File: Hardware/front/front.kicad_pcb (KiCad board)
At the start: 4 copper layers, 177 x 62 mm, 67 parts, among them J102 Conn_02x25_Counter_Clockwise, J301 Conn_02x25_Counter_Clockwise, Q301 2N7002E, Q302 2N7002E, SW201 B3W-9002-Y1C, SW202 B3W-9002-Y1C, SW203 B3W-9002-Y1C, SW204 B3W-9002-Y1C, SW205 B3W-9000-RHG2C, SW206 B3W-9002-G1G, SW207 TT EN11, U101 XRA1203, U102 AT24CS32-XHM, U103 PCA9955B, U201 74LV14, U202 74LVC1G14GV

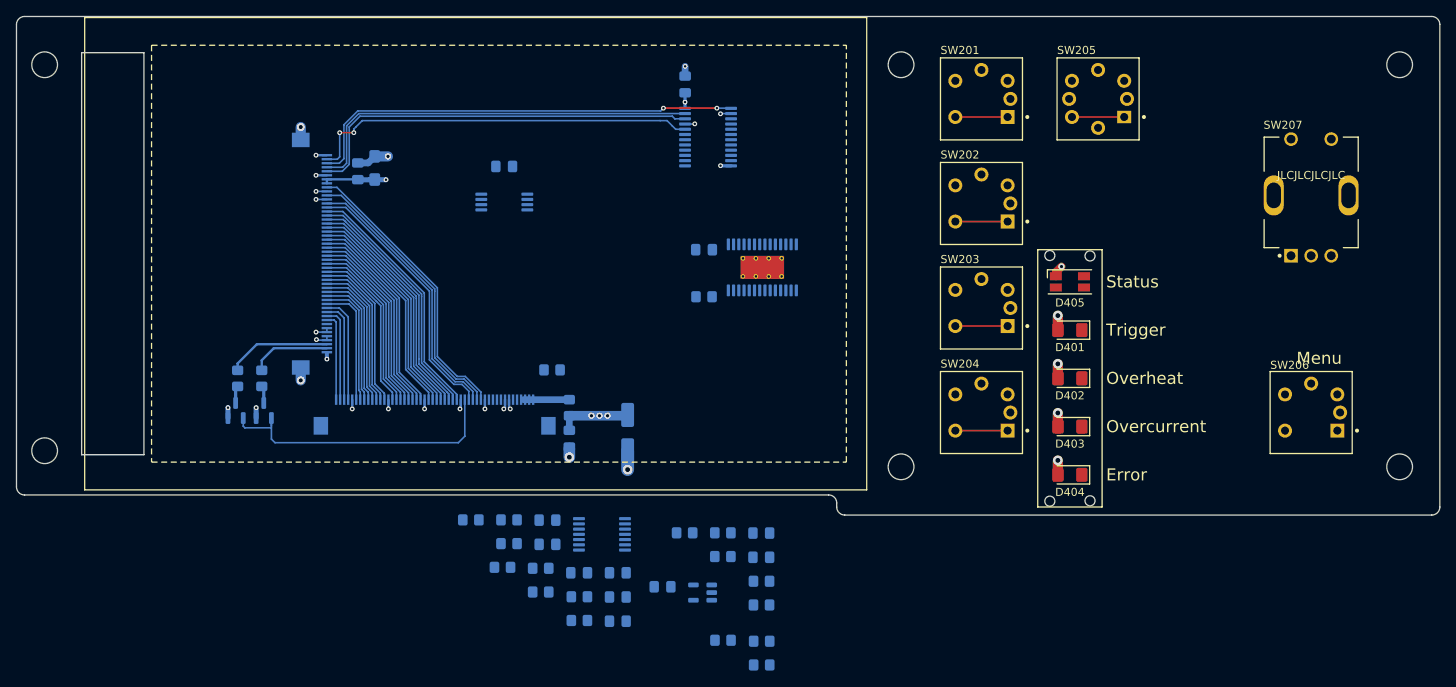
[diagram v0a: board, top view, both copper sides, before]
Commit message: More reworking of the controller and friends
- Add more rear IO to the controller, in this case finishing positioning
  of the Ethernet jack, and adding a suitable right angle USB B jack
  (USB C is preferrable but there's basically no jacks that are
  sufficiently long)

- Mostly finish power section on controller (save for the enable input
  for our +3V3 rail; it'll be slaved off the SoM +3V3 rail)

- Minor tweaks to pinout of FFC connector on front panel

- Update cutout shape of analog board

- Fixed a few footprints metadata

- Add footprints for further rear panel IO
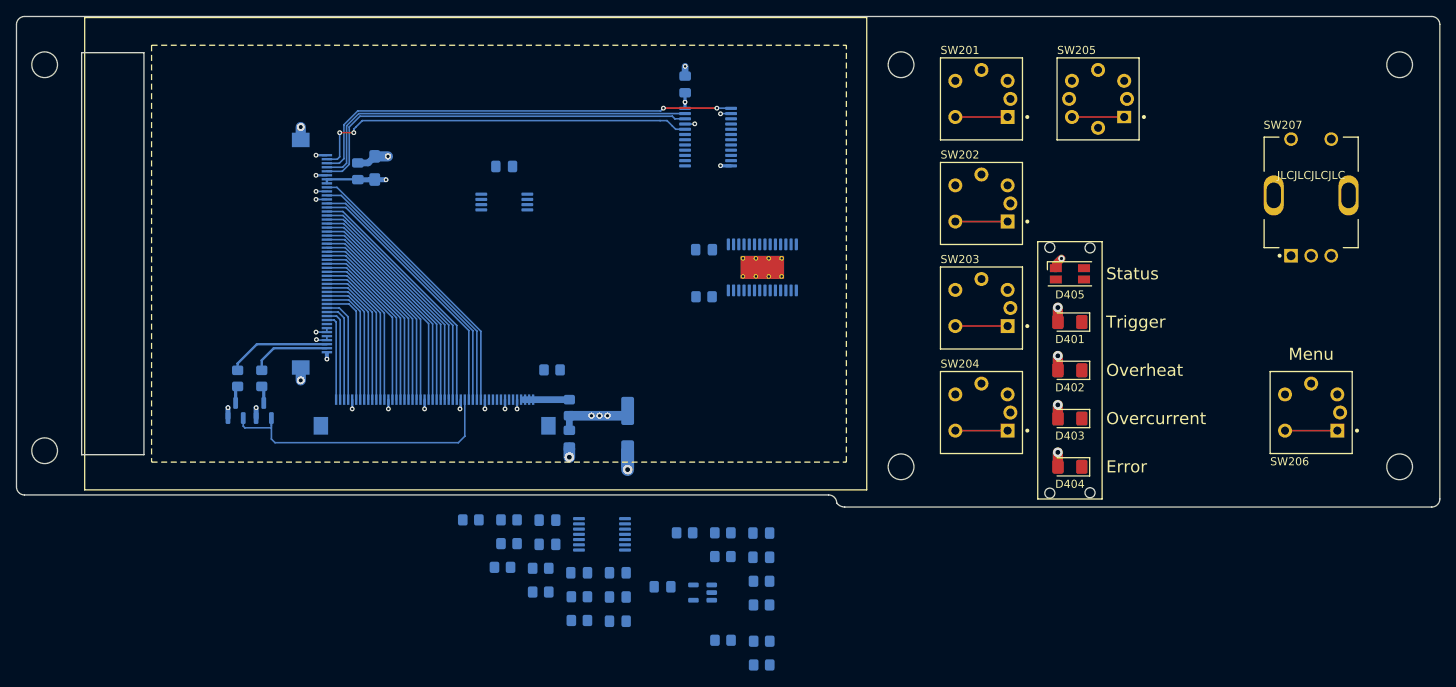
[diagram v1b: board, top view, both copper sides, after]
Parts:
- C102: footprint Capacitor_SMD:CP_Elec_5x5.3 -> Capacitor_SMD:CP_Elec_6.3x5.7
- moved D401 1.00 mm to (169.0, 57.0)
- moved D402 1.00 mm to (169.0, 63.0)
- moved D403 1.00 mm to (169.0, 69.0)
- moved D404 1.00 mm to (169.0, 75.0)
- moved D405 1.00 mm to (169.0, 51.0)
- moved REF** 1.00 mm to (169.0, 63.0)
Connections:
- J102 pad 5: unconnected-(J102-Pin_5) -> GND
- J102 pad 6: unconnected-(J102-Pin_6) -> /ENCODER_B
- J102 pad 7: GND -> /ENCODER_A
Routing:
- net Net-(R213-Pad2): track 0.00 -> 6.50 mm
- net /SPI_SCK: track 34.8 -> 34.2 mm
- net /~{SPI_CS}: track 35.6 -> 35.1 mm
- net /SPI_MISO: track 33.2 -> 32.6 mm
- net /SPI_MOSI: track 33.9 -> 33.3 mm
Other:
- board size 177 x 62 mm -> 177 x 61 mm

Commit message: Start routing front panel stuff
- Routed some of the LED driver pins and replaced footprints of passives
  with 0603 size to match the controller board
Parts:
- C101, C104, C105, C106, C201, C202, C203, C204, C205, C206, C207, C208, C209, C302: footprint Capacitor_SMD:C_0805_2012Metric_Pad1.18x1.45mm_HandSolder -> Capacitor_SMD:C_0603_1608Metric_Pad1.08x0.95mm_HandSolder
- C102: value 100µF -> 33µF
- R101, R102, R201, R202, R203, R204, R205, R206, R207, R208, R209, R210, R211, R212, R213, R214, R215, R216: footprint Resistor_SMD:R_0805_2012Metric_Pad1.20x1.40mm_HandSolder -> Resistor_SMD:R_0603_1608Metric_Pad0.98x0.95mm_HandSolder
- moved R102 37.1 mm to (118.5, 28.5), turned to 0 degrees
- moved U103 8.28 mm to (124.0, 55.0), turned to 180 degrees
- moved R101 5.43 mm to (126.0, 49.0), turned to 0 degrees
- moved C106 1.80 mm to (122.0, 49.0)
- moved C104 1.38 mm to (122.0, 28.5), turned to 180 degrees
- moved C105 0.95 mm to (98.7, 36.7)
- moved C202 0.47 mm to (112.8, 88.7)
- moved C203 0.47 mm to (112.8, 91.7)
- moved C205 0.47 mm to (112.8, 94.7)
- moved C207 0.47 mm to (108.0, 88.7)
- moved R206 0.47 mm to (108.0, 91.6)
- moved R214 0.47 mm to (108.0, 94.6)
- turned D405 to 180 degrees
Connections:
- U103 pad 14: /LED_EN_R -> /LED_MENU
- U103 pad 15: /LED_MENU -> /LED_STATUS_G
- U103 pad 16: /LED_STATUS_G -> /LED_STATUS_B
- U103 pad 17: unconnected-(U103-LED10) -> /LED_STATUS_R
- U103 pad 18: unconnected-(U103-LED11) -> /LED_TRIGGER
- U103 pad 20: /LED_TRIGGER -> /LED_MODE_EXT
- U103 pad 6: /LED_STATUS_B -> unconnected-(U103-LED0)
- U103 pad 7: /LED_STATUS_R -> unconnected-(U103-LED1)
- U103 pad 8: /LED_MODE_EXT -> unconnected-(U103-LED2)
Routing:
- net /LED_MENU: track 0.00 -> 93.9 mm, vias 0 -> 1
- net /LED_OVRHEAT: track 0.00 -> 77.0 mm, vias 0 -> 1
- net /LED_ERROR: track 0.00 -> 75.3 mm, vias 0 -> 1
- net /LED_OVRCURR: track 0.00 -> 74.3 mm, vias 0 -> 1
- net /LED_STATUS_R: track 0.00 -> 73.1 mm, vias 0 -> 1
- net /LED_TRIGGER: track 0.00 -> 68.7 mm, vias 0 -> 1
- net /LED_STATUS_B: track 0.00 -> 66.0 mm, vias 0 -> 1
- net /LED_STATUS_G: track 0.00 -> 63.4 mm, vias 0 -> 1
- net /LED_MODE_EXT: track 0.00 -> 56.9 mm, vias 0 -> 1
- net GND: track 31.0 -> 39.4 mm, vias 21 -> 23
- net +3V3: track 32.4 -> 36.2 mm, vias 14 -> 15
- net /~{IRQ}: track 55.6 -> 57.8 mm
- net Net-(U103-REXT): track 0.00 -> 1.77 mm

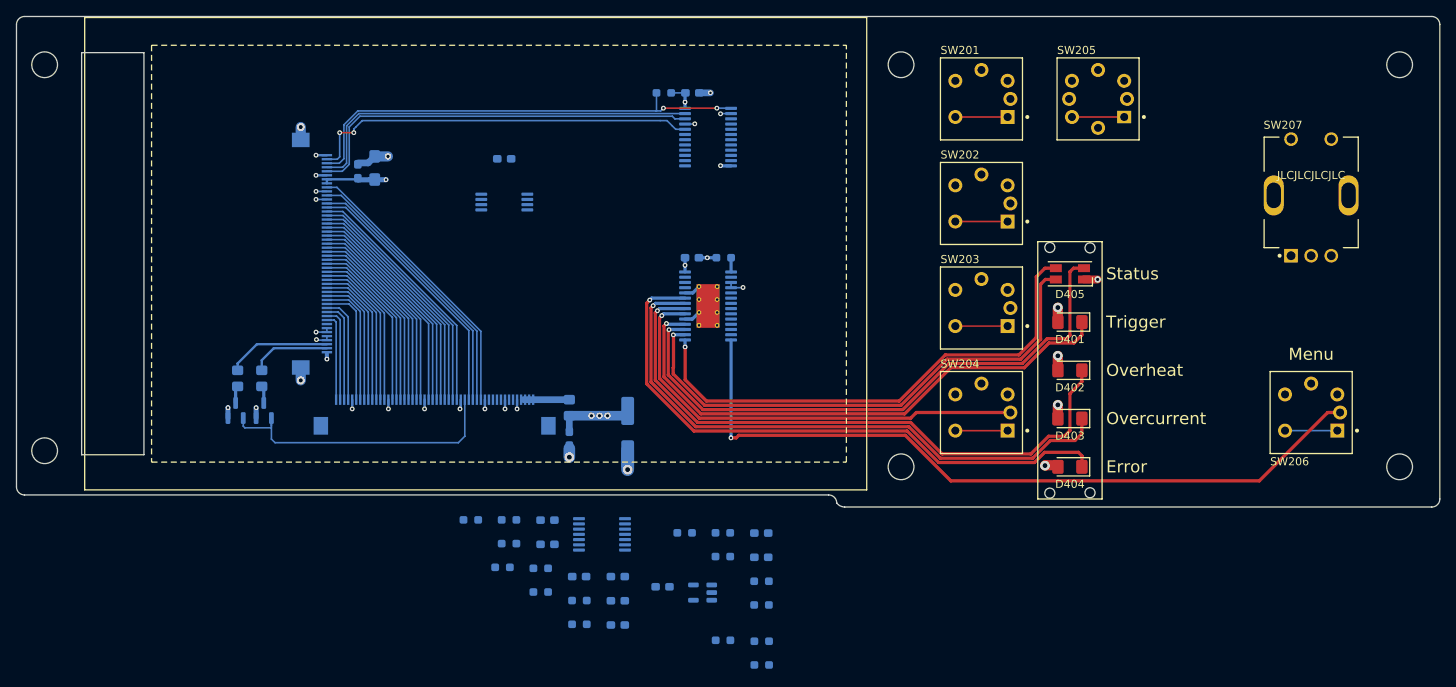
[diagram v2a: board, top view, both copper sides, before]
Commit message: Finished routing front panel
- Finished routing the contents of the front panel; it could probably
  use an optimization pass and general cleanup.

  A few of the assignments of IOs/LED driver outputs were changed as
  well to make the routing less of a pain in the ass, as compared to the
  previous front panels.

- Minor tweaks to controller to remove some unused signals
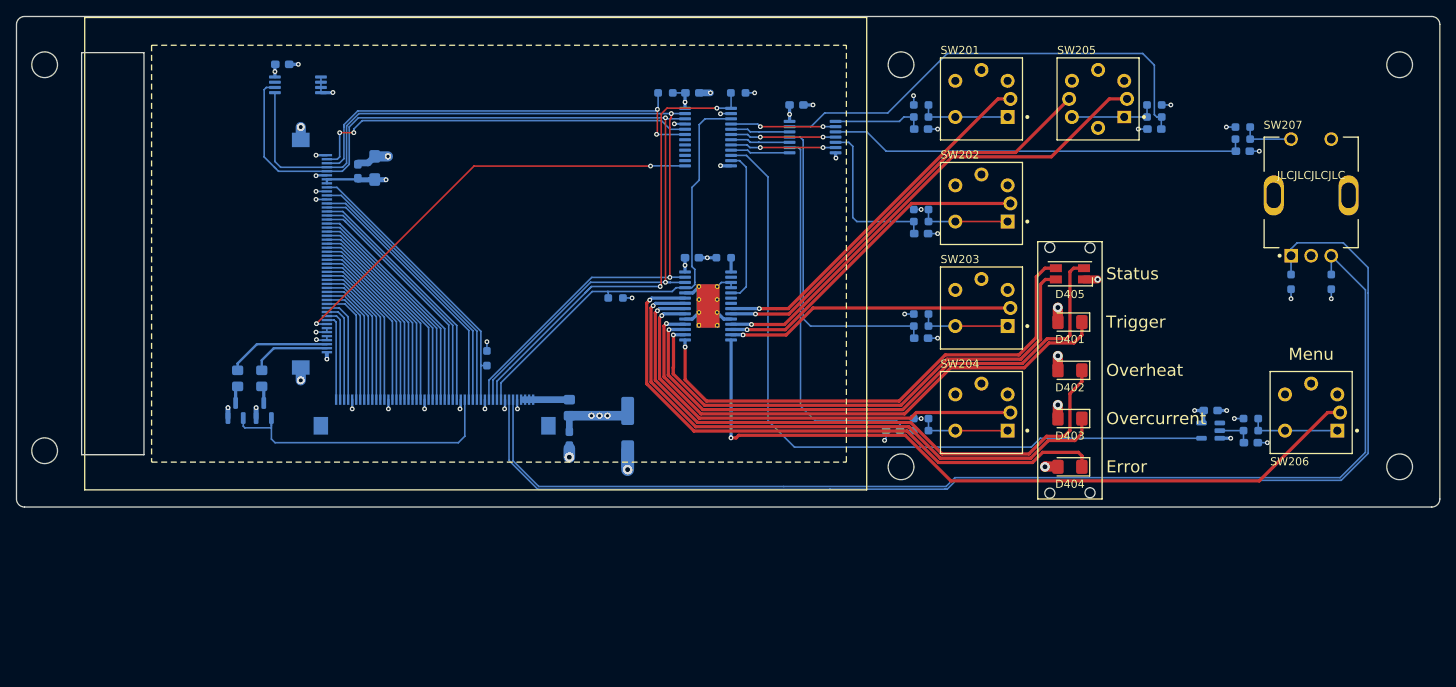
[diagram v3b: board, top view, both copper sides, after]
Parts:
- removed R211, R212: 10k, Resistor_SMD:R_0603_1608Metric_Pad0.98x0.95mm_HandSolder
- added R103: 10k, Resistor_SMD:R_0603_1608Metric_Pad0.98x0.95mm_HandSolder, B.Cu at (112.5, 54.0)
- added R104: 10k, Resistor_SMD:R_0603_1608Metric_Pad0.98x0.95mm_HandSolder, B.Cu at (96.5, 61.5)
- added R217: 10k, Resistor_SMD:R_0603_1608Metric_Pad0.98x0.95mm_HandSolder, B.Cu at (196.5, 52.0)
- added R218: 10k, Resistor_SMD:R_0603_1608Metric_Pad0.98x0.95mm_HandSolder, B.Cu at (201.5, 52.0)
- added R303: 10k, Resistor_SMD:R_0603_1608Metric_Pad0.98x0.95mm_HandSolder, B.Cu at (118.7, 28.5)
- moved R216 103.9 mm to (190.5, 34.2)
- moved R214 103.1 mm to (190.5, 32.8)
- moved R210 94.6 mm to (179.5, 31.5), turned to 0 degrees
- moved C205 90.9 mm to (179.5, 33.0)
- moved C208 90.2 mm to (190.5, 35.8), turned to 0 degrees
- moved C209 88.4 mm to (191.5, 72.0), turned to 0 degrees
- moved R205 85.5 mm to (179.5, 30.0), turned to 0 degrees
- moved C207 81.2 mm to (186.5, 68.0), turned to 0 degrees
- moved R206 73.6 mm to (150.5, 31.5)
- moved R201 72.4 mm to (150.5, 30.0)
- moved R213 71.5 mm to (191.5, 70.5), turned to 0 degrees
- moved R202 68.0 mm to (150.5, 43.0)
- moved R215 67.2 mm to (191.5, 69.0)
- moved U202 66.3 mm to (186.5, 70.5)
- moved R203 58.7 mm to (150.5, 56.0)
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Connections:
- C201 pad 1: Net-(C201-Pad1) -> Net-(U201-Pad1)
- C203 pad 1: Net-(C203-Pad1) -> Net-(U201-Pad11)
- J301 pad 48: /~{IRQ} -> /~{TOUCH_IRQ}
- R206 pad 2: Net-(C201-Pad1) -> Net-(U201-Pad1)
- R208 pad 2: Net-(C203-Pad1) -> Net-(U201-Pad11)
- U101 pad 10: /SW_MODE_EXT -> /SW_MENU
- U101 pad 13: unconnected-(U101-P8) -> /~{DISP_RESET}
- U101 pad 19: unconnected-(U101-P14) -> /~{TOUCH_IRQ}
- U101 pad 4: /SW_MENU -> /SW_MODE_CC
- U101 pad 5: /SW_ENCODER -> /SW_ENABLE
- U101 pad 6: /SW_ENABLE -> /SW_ENCODER
- U101 pad 7: /SW_MODE_CC -> /SW_MODE_CW
- U101 pad 9: /SW_MODE_CW -> /SW_MODE_EXT
- U103 pad 11: /LED_MODE_CV -> /LED_EN_R
- U103 pad 12: /LED_MODE_CC -> /LED_MODE_CV
- U103 pad 13: /LED_EN_G -> /LED_MODE_CW
- U103 pad 8: unconnected-(U103-LED2) -> /LED_MODE_CC
- U103 pad 9: /LED_MODE_CW -> /LED_EN_G
- U201 pad 1: Net-(C208-Pad1) -> Net-(U201-Pad1)
- U201 pad 10: /SW_MODE_CV -> /SW_MODE_CW
- U201 pad 11: Net-(C202-Pad1) -> Net-(U201-Pad11)
- U201 pad 2: /SW_ENCODER -> /SW_MODE_CC
- U201 pad 3: Net-(C201-Pad1) -> Net-(C208-Pad1)
- U201 pad 4: /SW_MODE_CC -> /SW_ENCODER
- U201 pad 5: Net-(C203-Pad1) -> Net-(C202-Pad1)
- U201 pad 6: /SW_MODE_CW -> /SW_MODE_CV
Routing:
- net /ENCODER_A: track 0.00 -> 155.2 mm
- net /ENCODER_B: track 0.00 -> 145.2 mm
- net /SW_MENU: track 0.00 -> 91.7 mm
- net /SCL: track 50.2 -> 120.7 mm, vias 0 -> 2
- net /SDA: track 50.0 -> 117.9 mm, vias 0 -> 2
- net /LED_EN_R: track 0.00 -> 60.9 mm, vias 0 -> 1
- net Net-(C205-Pad1): track 0.00 -> 58.4 mm
- net /~{RESET}: track 0.00 -> 56.7 mm
- net /~{DISP_RESET}: track 0.00 -> 55.3 mm, vias 0 -> 2
- net /~{TOUCH_IRQ}: track 0.00 -> 55.1 mm, vias 0 -> 2
- net /LED_EN_G: track 0.00 -> 53.1 mm, vias 0 -> 1
- net Net-(C208-Pad1): track 0.00 -> 52.3 mm
- net Net-(C204-Pad1): track 0.00 -> 49.2 mm
- net /LED_MODE_CC: track 0.00 -> 45.5 mm, vias 0 -> 1
- net /LED_MODE_CV: track 0.00 -> 41.3 mm, vias 0 -> 1
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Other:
- outline, holes or cut-outs redrawn

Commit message: Minor front panel tweaks
- Switched IO expander out for PCA9535 (easier to get replacement parts
  for, and (mostly) pin compatible with the XRA1200 we used before)

- Minor layout changes
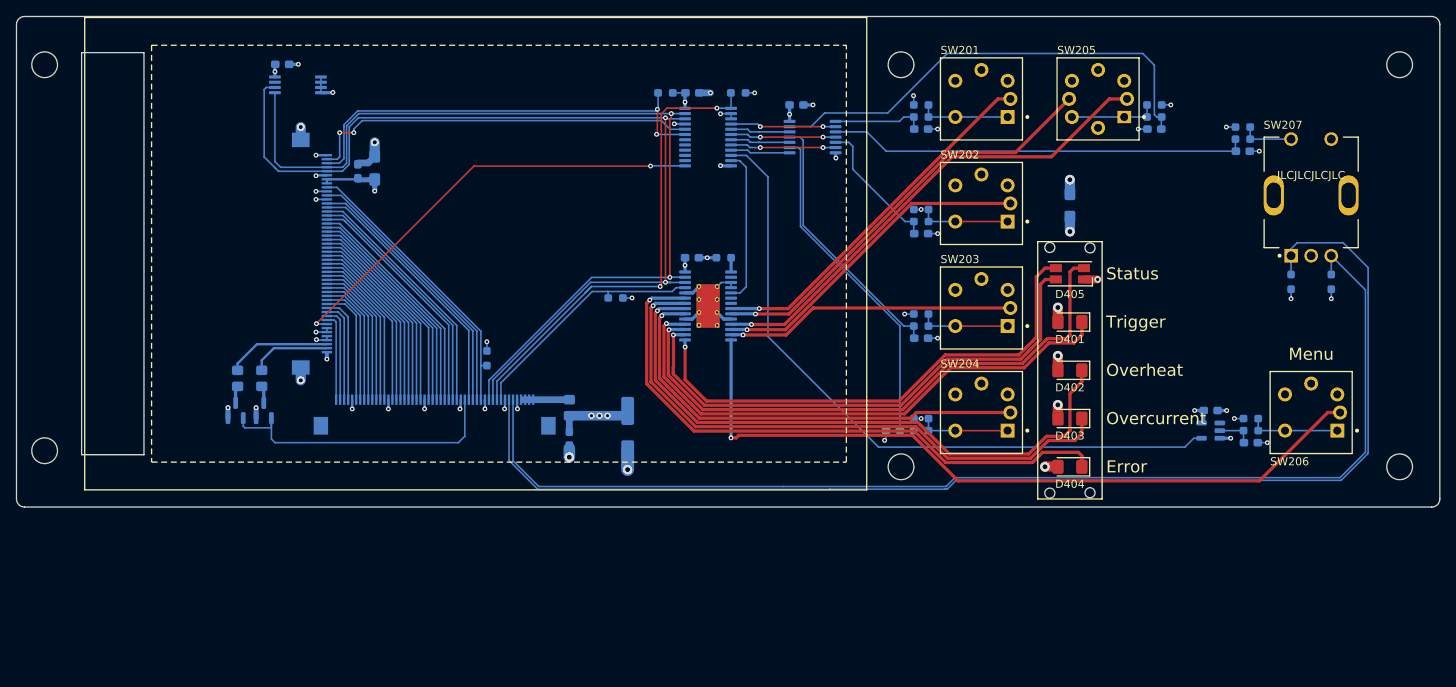
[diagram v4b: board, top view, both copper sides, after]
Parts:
- added C401: 10µF, Capacitor_Tantalum_SMD:CP_EIA-3216-18_Kemet-A_Pad1.58x1.35mm_HandSolder, B.Cu at (169.0, 42.5)
- U101: value XRA1203 -> PCA9535PW
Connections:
- U101 pad 3: /~{RESET} -> GND
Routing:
- net /~{RESET}: track 56.7 -> 30.7 mm
- net Net-(U201-Pad11): track 39.7 -> 32.9 mm
- net /SW_MENU: track 91.7 -> 85.6 mm
- net Net-(C204-Pad1): track 49.2 -> 43.3 mm
- net Net-(C202-Pad1): track 20.5 -> 17.0 mm
- net GND: track 59.4 -> 61.9 mm, vias 35 -> 36
- net +3V3: track 55.9 -> 57.8 mm, vias 30 -> 31

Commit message: Analog board layout
- Started work on adding the voltage sense circuitry, including the
  selector relay, IO expander to drive the relay, and the second ADC to
  convert the voltage values

- Changed the layout of analog board to better take advantage of
  available space

- Minor changes to front panel layout for aesthetics
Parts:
- R301, R302: footprint Resistor_SMD:R_0805_2012Metric_Pad1.20x1.40mm_HandSolder -> Resistor_SMD:R_0603_1608Metric_Pad0.98x0.95mm_HandSolder
